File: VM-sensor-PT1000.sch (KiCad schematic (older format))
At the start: 16 parts, among them P1 PT100, P2 CONN_01X03, U1 AMS1117, U2 MCP6001

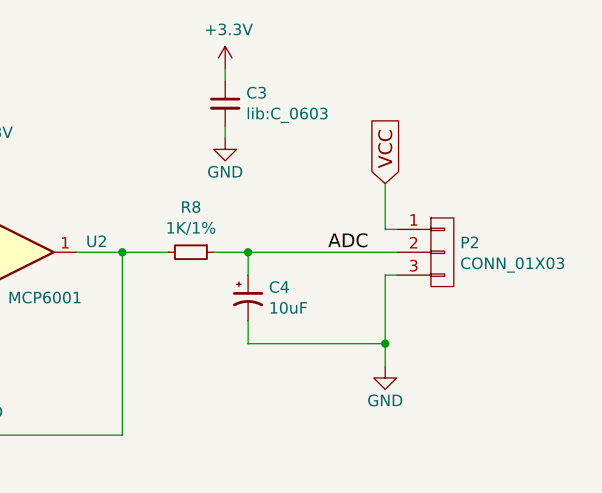
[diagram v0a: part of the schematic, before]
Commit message: change component 0603 to 0805 & header
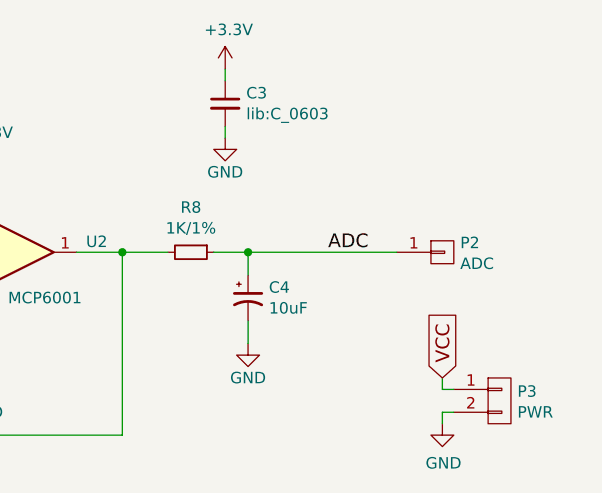
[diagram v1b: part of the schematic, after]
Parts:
- removed P2: CONN_01X03, Pin_Headers:Pin_Header_Straight_1x03, symbol CONN_01X03
- added P2: ADC, Pin_Headers:Pin_Header_Straight_1x01, symbol CONN_01X01
- added P3: PWR, Pin_Headers:Pin_Header_Straight_1x02, symbol CONN_01X02
- C1, C2, C4: footprint lib:C_0603 -> Capacitors_SMD:C_0805
- C3: footprint (none) -> Capacitors_SMD:C_0805
- P1: footprint Pin_Headers:Pin_Header_Straight_1x03 -> Connectors_Hirose:Hirose_DF63-3P-3.96DSA_03x3.96mm_Straight
- R1, R2, R3, R4, R5, R6, R7, R8: footprint lib:R_0603 -> Resistors_SMD:R_0805
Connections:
- net ADC: now also P2.1 (P1)
- net GND: now also P3.2 (P2)
- net VCC: now also P3.1 (P1)
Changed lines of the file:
@@
 F 0 "P1" H 5400 2850 50  0000 C CNN
 F 1 "PT100" H 5400 3300 50  0000 C CNN
-F 2 "Pin_Headers:Pin_Header_Straight_1x03" H 5400 3050 50  0001 C CNN
+F 2 "Connectors_Hirose:Hirose_DF63-3P-3.96DSA_03x3.96mm_Straight" H 5400 3050 50  0001 C CNN
 F 3 "" H 5400 3050 50  0000 C CNN
 	1    5400 3050
 	-1   0    0    1
-$EndComp
-$Comp
-L CONN_01X03 P2
-U 1 1 585E3749
-P 9750 3050
-F 0 "P2" H 9828 3091 50  0000 L CNN
-F 1 "CONN_01X03" H 9828 3000 50  0000 L CNN
-F 2 "Pin_Headers:Pin_Header_Straight_1x03" H 9750 3050 50  0001 C CNN
-F 3 "" H 9750 3050 50  0000 C CNN
-	1    9750 3050
-	1    0    0    -1
 $EndComp
 $Comp
@@
 F 0 "R1" H 6409 2696 50  0000 L CNN
 F 1 "3.3K/1%" H 6409 2605 50  0000 L CNN
-F 2 "lib:R_0603" H 6350 2650 50  0001 C CNN
+F 2 "Resistors_SMD:R_0805" H 6350 2650 50  0001 C CNN
 F 3 "" H 6350 2650 50  0000 C CNN
 	1    6350 2650
@@
 F 0 "R7" V 7350 3400 50  0000 C CNN
 F 1 "100K/1%" V 7550 3400 50  0000 C CNN
-F 2 "lib:R_0603" H 7450 3400 50  0001 C CNN
+F 2 "Resistors_SMD:R_0805" H 7450 3400 50  0001 C CNN
 F 3 "" H 7450 3400 50  0000 C CNN
 	1    7450 3400
@@
 	1    0    0    -1
 $EndComp
-Text GLabel 9500 2750 1    60   Input ~ 0
+Text GLabel 9750 3600 1    60   Input ~ 0
 VCC
 $Comp
 L GND #PWR02
 U 1 1 585E400C
-P 9500 3550
-F 0 "#PWR02" H 9500 3300 50  0001 C CNN
-F 1 "GND" H 9500 3400 50  0000 C CNN
-F 2 "" H 9500 3550 50  0000 C CNN
-F 3 "" H 9500 3550 50  0000 C CNN
-	1    9500 3550
+P 8900 3450
+F 0 "#PWR02" H 8900 3200 50  0001 C CNN
+F 1 "GND" H 8900 3300 50  0000 C CNN
+F 2 "" H 8900 3450 50  0000 C CNN
+F 3 "" H 8900 3450 50  0000 C CNN
+	1    8900 3450
 	1    0    0    -1
 $EndComp
@@
 F 0 "R8" V 8454 3050 50  0000 C CNN
 F 1 "1K/1%" V 8545 3050 50  0000 C CNN
-F 2 "lib:R_0603" H 8650 3050 50  0001 C CNN
+F 2 "Resistors_SMD:R_0805" H 8650 3050 50  0001 C CNN
 F 3 "" H 8650 3050 50  0000 C CNN
 	1    8650 3050
@@
 F 0 "C4" H 8991 3296 50  0000 L CNN
 F 1 "10uF" H 8991 3205 50  0000 L CNN
-F 2 "lib:C_0603" H 8900 3250 50  0001 C CNN
+F 2 "Capacitors_SMD:C_0805" H 8900 3250 50  0001 C CNN
 F 3 "" H 8900 3250 50  0000 C CNN
 	1    8900 3250
@@
 F 0 "R4" H 7009 2696 50  0000 L CNN
 F 1 "3.3K/1%" H 7009 2605 50  0000 L CNN
-F 2 "lib:R_0603" H 6950 2650 50  0001 C CNN
+F 2 "Resistors_SMD:R_0805" H 6950 2650 50  0001 C CNN
 F 3 "" H 6950 2650 50  0000 C CNN
 	1    6950 2650
@@
 F 0 "R2" H 6409 3446 50  0000 L CNN
 F 1 "100/1%" H 6409 3355 50  0000 L CNN
-F 2 "lib:R_0603" H 6350 3400 50  0001 C CNN
+F 2 "Resistors_SMD:R_0805" H 6350 3400 50  0001 C CNN
 F 3 "" H 6350 3400 50  0000 C CNN
 	1    6350 3400
@@
 F 0 "R3" V 6700 3150 50  0000 C CNN
 F 1 "1K/1%" V 6900 3150 50  0000 C CNN
-F 2 "lib:R_0603" H 6800 3150 50  0001 C CNN
+F 2 "Resistors_SMD:R_0805" H 6800 3150 50  0001 C CNN
 F 3 "" H 6800 3150 50  0000 C CNN
 	1    6800 3150
@@
 F 0 "R5" V 6950 3400 50  0000 C CNN
 F 1 "100K/1%" V 7150 3400 50  0000 C CNN
-F 2 "lib:R_0603" H 7050 3400 50  0001 C CNN
+F 2 "Resistors_SMD:R_0805" H 7050 3400 50  0001 C CNN
 F 3 "" H 7050 3400 50  0000 C CNN
 	1    7050 3400
@@
 	7750 3600 7750 3350
 Wire Wire Line
-	9500 2750 9500 2950
-Wire Wire Line
-	9500 2950 9550 2950
-Wire Wire Line
-	9550 3150 9500 3150
-Wire Wire Line
-	9500 3150 9500 3550
-Wire Wire Line
 	1950 2900 1950 2950
 Wire Wire Line
@@
 Wire Wire Line
 	8900 3350 8900 3450
-Wire Wire Line
-	8900 3450 9500 3450
-Connection ~ 9500 3450
 Wire Wire Line
 	5600 3050 5900 3050
@@
 F 0 "C3" H 8892 2446 50  0000 L CNN
 F 1 "lib:C_0603" H 8892 2355 50  0000 L CNN
-F 2 "" H 8800 2400 50  0000 C CNN
+F 2 "Capacitors_SMD:C_0805" H 8800 2400 50  0001 C CNN
 F 3 "" H 8800 2400 50  0000 C CNN
 	1    8800 2400
@@
 F 0 "C1" H 2492 3196 50  0000 L CNN
 F 1 "10uF/25v" H 2492 3105 50  0000 L CNN
-F 2 "lib:C_0603" H 2400 3150 50  0001 C CNN
+F 2 "Capacitors_SMD:C_0805" H 2400 3150 50  0001 C CNN
 F 3 "" H 2400 3150 50  0000 C CNN
 	1    2400 3150
@@
 F 0 "C2" H 4342 3246 50  0000 L CNN
 F 1 "10uF/25v" H 4342 3155 50  0000 L CNN
-F 2 "lib:C_0603" H 4250 3200 50  0001 C CNN
+F 2 "Capacitors_SMD:C_0805" H 4250 3200 50  0001 C CNN
 F 3 "" H 4250 3200 50  0000 C CNN
 	1    4250 3200
@@
 F 0 "R6" V 7150 2950 50  0000 C CNN
 F 1 "1K/1%" V 7350 2950 50  0000 C CNN
-F 2 "lib:R_0603" H 7250 2950 50  0001 C CNN
+F 2 "Resistors_SMD:R_0805" H 7250 2950 50  0001 C CNN
 F 3 "" H 7250 2950 50  0000 C CNN
 	1    7250 2950
@@
 Text Label 9250 3050 0    60   ~ 0
 ADC
+$Comp
+L CONN_01X02 P3
+U 1 1 58609B23
+P 10000 3700
+F 0 "P3" H 10078 3741 50  0000 L CNN
+F 1 "PWR" H 10078 3650 50  0000 L CNN
+F 2 "Pin_Headers:Pin_Header_Straight_1x02" H 10000 3700 50  0001 C CNN
+F 3 "" H 10000 3700 50  0000 C CNN
+	1    10000 3700
+	1    0    0    -1
+$EndComp
+$Comp
+L CONN_01X01 P2
+U 1 1 58609B7F
+P 9750 3050
+F 0 "P2" H 9828 3091 50  0000 L CNN
+F 1 "ADC" H 9828 3000 50  0000 L CNN
+F 2 "Pin_Headers:Pin_Header_Straight_1x01" H 9750 3050 50  0001 C CNN
+F 3 "" H 9750 3050 50  0000 C CNN
+	1    9750 3050
+	1    0    0    -1
+$EndComp
+Wire Wire Line
+	9750 3600 9750 3650
+Wire Wire Line
+	9750 3650 9800 3650
+$Comp
+L GND #PWR010
+U 1 1 5860A0C0
+P 9750 3800
+F 0 "#PWR010" H 9750 3550 50  0001 C CNN
+F 1 "GND" H 9755 3627 50  0000 C CNN
+F 2 "" H 9750 3800 50  0000 C CNN
+F 3 "" H 9750 3800 50  0000 C CNN
+	1    9750 3800
+	1    0    0    -1
+$EndComp
+Wire Wire Line
+	9800 3750 9750 3750
+Wire Wire Line
+	9750 3750 9750 3800
 $EndSCHEMATC

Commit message: Completed PCB
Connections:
- net Red renamed Blue
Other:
- moved on the sheet: C1, C2, C3, C4, P1, P2, P3, R1, R2, R3, R4, R5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
